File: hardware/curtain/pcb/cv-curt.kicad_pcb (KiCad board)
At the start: 2 copper layers, 88.7 x 99.9 mm, 45 parts, among them J1 2P 5.08mm, J2 3P 5.08mm, K1 SRD-05VDC-SL-C, K2 SRD-05VDC-SL-C, Q1 S8050, Q2 S8050, SW1 Tactile 6mm, SW2 Tactile 6mm, SW3 Tactile 6mm, U1 ESP32-WROOM-32E (4MB), U2 AMS1117-3.3, U3 PC817, U4 PC817

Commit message: hardware: fix mains isolation barrier gaps, add load-controller PCB
Adds the 13th board (ultra-compact dual-channel load controller: ESP32-C3,
opto+relay channel, MOSFET PWM channel, USB-C, AP2112K LDO, USBLC6 ESD) and
regenerates all 12 existing boards, which were stale with respect to earlier
relay-pinout and LED-polarity fixes.

The substantive change is to the mains isolation barrier. It is a keepout band
the router must not cross, deliberately cut where a component straddles it
because there the isolation is provided by the part's package. Three linked
defects made those cuts unsafe, each only visible once the previous was fixed:

1. The cut removed the barrier across the full band width for the straddling
   part's whole height, while the ISO_BRIDGE area that excuses the gap covered
   only the part itself. The router used the leftover strip beside the part to
   bring +5V within 6.99 mm of AC_N against an 8.0 mm reinforced creepage rule.
2. Straddling parts can overlap in y, so cutting per part put one part's
   keepout on another part's pads. The exempt x-ranges are now unioned per
   strip by a sweep line.
3. The rule only relaxes for items insideArea('ISO_BRIDGE'). With the hole the
   same size as the area, a track could hug the hole's edge without being
   contained in it, so the rule fired anyway and the router had no way to know.
   The hole is now the part's pad bbox + 0.3 mm, strictly inside ISO_BRIDGE at
   the footprint bbox + 0.6 mm.

The tighter hole leaves mains nets less room to reach bridge pads, so some
boards report more unconnected items. That is deliberate: those are documented
hand-routing items, whereas a creepage violation is a safety defect.

Also fixed in the generator:
- _pad_shape() derived a pad's layers from PAD::GetLayer(), which returns F.Cu
  even for pads on B.Cu. Every back-side pad became a phantom obstacle on the
  front, blocking legal paths there while hiding the real one behind. Only
  IsOnLayer() is truthful.
- Castella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
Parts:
- moved D2 47.5 mm to (163.7, 164.5)
- moved R2 47.5 mm to (171.8, 154.3)
- moved R5 47.5 mm to (158.6, 157.3)
- moved R8 47.5 mm to (178.4, 163.2)
- moved U2 47.5 mm to (170.3, 166.7)
- moved C2 47.5 mm to (175.6, 154.5)
- moved C3 47.5 mm to (153.0, 136.8)
- moved C4 47.5 mm to (157.5, 136.8)
- moved C5 47.5 mm to (174.6, 151.3)
- moved C6 47.5 mm to (158.6, 154.3)
- moved JP 47.5 mm to (168.2, 154.7)
- moved LED0 47.5 mm to (152.5, 156.3)
- moved LED2 47.5 mm to (152.5, 161.8)
- moved R1 47.5 mm to (179.1, 151.2)
- moved R10 47.5 mm to (153.0, 164.7)
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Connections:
- K1 pad 2: MOTOR_OPEN_PIN_SW -> +5V
- K1 pad 3: +5V -> MOTOR_OPEN_PIN_SW
- K1 pad 4: MOTOR_OPEN_PIN_COIL -> N$K1.4
- K1 pad 5: N$K1.5 -> MOTOR_OPEN_PIN_COIL
- K2 pad 2: MOTOR_CLOSE_PIN_SW -> +5V
- K2 pad 3: +5V -> MOTOR_CLOSE_PIN_SW
- K2 pad 4: MOTOR_CLOSE_PIN_COIL -> N$K2.4
- K2 pad 5: N$K2.5 -> MOTOR_CLOSE_PIN_COIL
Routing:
- net MOTOR_CLOSE_PIN_SW: track 71.5 -> 0.00 mm
- net AC_L_FUSED: track 92.4 -> 23.7 mm
- net AC_N: track 118.4 -> 51.3 mm
- net BTN_STOP: track 88.4 -> 37.5 mm, vias 3 -> 0
- net +3V3: track 193.3 -> 144.2 mm
- net BTN_OPEN: track 104.5 -> 63.2 mm, vias 4 -> 2
- net MOTOR_OPEN_PIN: track 97.8 -> 58.3 mm
- net MOTOR_CLOSE_PIN: track 75.6 -> 45.6 mm, vias 3 -> 1
- net MOTOR_OPEN_PIN_SW: track 28.0 -> 0.00 mm
- net MOTOR_CLOSE_PIN_COIL: track 64.9 -> 49.3 mm
- net BTN_CLOSE: track 77.6 -> 92.9 mm, vias 4 -> 2
- net UART_RX: track 39.3 -> 54.0 mm
- net EN: track 54.6 -> 68.6 mm
- net +5V: track 199.7 -> 188.1 mm, vias 0 -> 1
- net UART_TX: track 44.5 -> 53.2 mm, vias 4 -> 0
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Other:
- outline, holes or cut-outs redrawn
- board text removed: "!! MAINS !!"

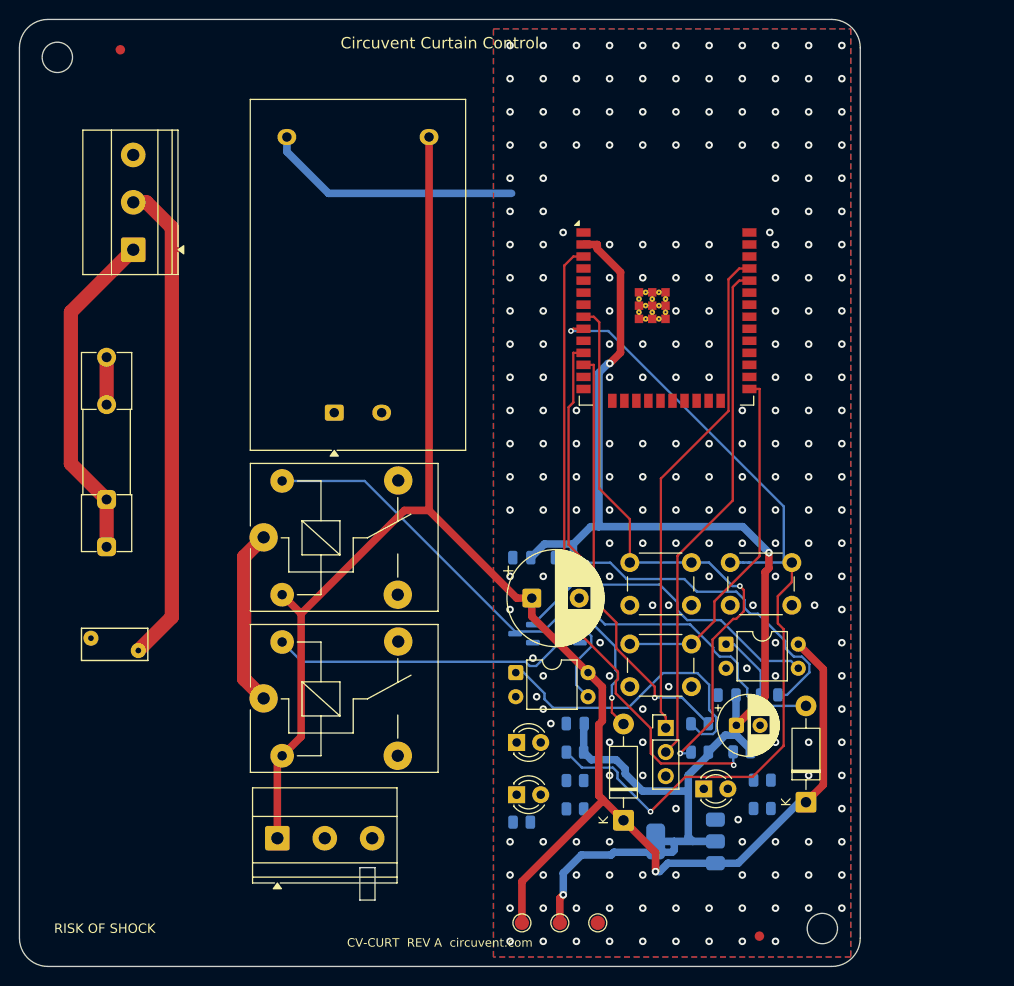
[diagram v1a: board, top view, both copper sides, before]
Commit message: Release 1.10.0, and stop shipping permissions the app never uses
Cut 1.10.0 (versionCode 12) and built it: AAB 38 MB, APK 83 MB, signed with the
upload key, JS bundle embedded.

Checking the generated manifest before writing the Play listing turned up
permissions no one had asked for. Every one of them is printed on the store page
for users to read before they install:

  RECORD_AUDIO          expo-camera asks for the microphone so video can be
                        recorded with sound. This app only ever puts the camera
                        in barcode mode to read a QR label, and expo-speech is
                        output-only - it speaks, it does not listen. Left in,
                        Play lists "Microphone" against a home-control app,
                        which is alarming, unexplainable and untrue.
  SYSTEM_ALERT_WINDOW   React Native's development overlay, useless in a release
                        build and shown to users as "Display over other apps".
  READ/WRITE_EXTERNAL_STORAGE
                        Legacy storage access nothing here touches.

Stripped via android.blockedPermissions. That emits tools:node="remove", which
is a merge instruction rather than a guarantee, so it was checked against the
finished artifact with aapt2 rather than the source manifest - all four are
absent from the APK.

NEARBY_WIFI_DEVICES now carries neverForLocation. Android otherwise treats it as
location-capable, because knowing which networks are in range is enough to place
someone, and Play's data safety review treats it the same way. The app uses it
only to join a new device's setup hotspot. That flag is a promise, so the plugin
says plainly that it has to come off if scan results are ever used positionally.

What is left is defensible: location for Wi-Fi onboarding (Android requires it),
camera for the QR label, nearby-devices flagged as non-positional.

Added mobile/store/listing with the text Play asks for - title, short and full
descriptions, and what'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
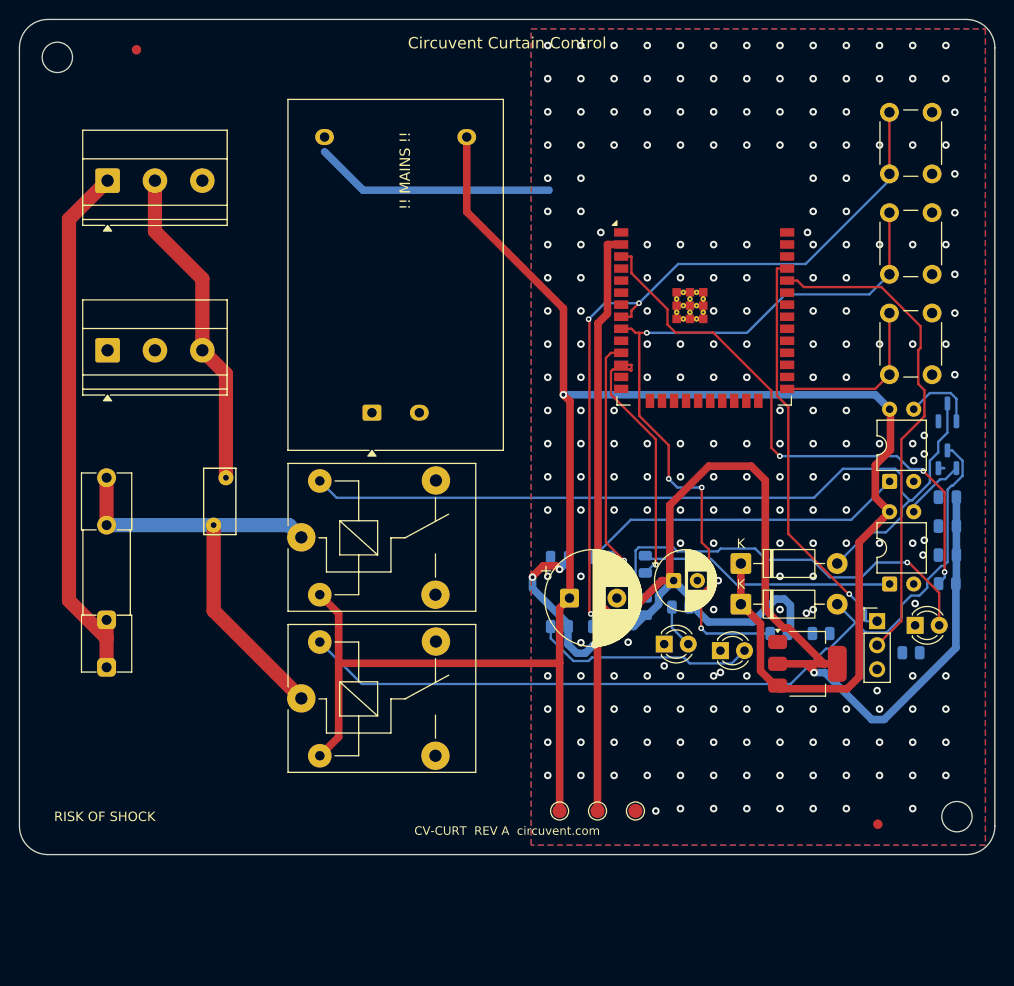
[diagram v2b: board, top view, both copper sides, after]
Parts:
- U2: moved to F.Cu
- moved J2 54.5 mm to (109.3, 114.9)
- moved Q1 50.4 mm to (197.9, 121.5), turned to 90 degrees
- moved SW1 49.3 mm to (191.8, 96.3), turned to 90 degrees
- moved C3 45.3 mm to (197.9, 130.4)
- moved R10 44.8 mm to (194.1, 146.8)
- moved LED0 43.8 mm to (194.5, 143.9)
- moved Q2 43.8 mm to (197.9, 126.4), turned to 90 degrees
- moved C4 40.5 mm to (197.9, 133.4)
- moved U4 40.5 mm to (191.8, 139.6), turned to 90 degrees
- moved SW3 39.5 mm to (191.8, 117.5), turned to 90 degrees
- moved SW2 34.7 mm to (191.8, 106.9), turned to 90 degrees
- moved R9 31.9 mm to (184.6, 144.8)
- moved R3 28.0 mm to (197.9, 139.5)
- moved C5 27.6 mm to (197.9, 136.5)
- moved R6 26.8 mm to (157.0, 144.0)
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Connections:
- J1 pad 3: MOTOR_CLOSE_PIN_SW -> PE
- J2 pad 1: +5V -> MOTOR_OPEN_PIN_SW
- J2 pad 2: MOTOR_OPEN_PIN_SW -> MOTOR_CLOSE_PIN_SW
- LED0 pad 1: N$LED0.1 -> GND
- LED0 pad 2: N$LED0.2 -> LED0_A
- LED1 pad 1: N$LED1.1 -> GND
- LED1 pad 2: N$LED1.2 -> LED1_A
- LED2 pad 1: N$LED2.1 -> GND
- LED2 pad 2: N$LED2.2 -> LED2_A
- R4 pad 2: BTN_OPEN -> LED0_A
- R5 pad 2: BTN_CLOSE -> LED1_A
- R6 pad 1: N$R6.1 -> +3V3
- R6 pad 2: N$R6.2 -> LED2_A
- R7 pad 1: N$R7.1 -> +3V3
- R7 pad 2: N$R7.2 -> BTN_OPEN
- R8 pad 1: N$R8.1 -> +3V3
- R8 pad 2: N$R8.2 -> BTN_CLOSE
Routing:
- net +3V3: track 144.2 -> 203.6 mm, vias 3 -> 4
- net LED0_A: track 0.00 -> 44.5 mm, vias 0 -> 1
- net MOTOR_CLOSE_PIN_COIL: track 49.3 -> 91.7 mm, vias 1 -> 0
- net MOTOR_OPEN_PIN: track 58.3 -> 25.6 mm
- net MOTOR_OPEN_PIN_OPT: track 7.34 -> 34.6 mm
- net MOTOR_OPEN_PIN_DRV: track 33.9 -> 7.83 mm
- net AC_L_FUSED: track 23.7 -> 48.2 mm
- net LED2_A: track 0.00 -> 23.7 mm
- net MOTOR_OPEN_PIN_COIL: track 68.4 -> 89.6 mm
- net AC_L: track 35.6 -> 56.6 mm
- net +5V: track 188.1 -> 207.8 mm
- net BTN_STOP: track 37.5 -> 17.9 mm
- net MOTOR_CLOSE_PIN: track 45.6 -> 27.8 mm
- net BTN_OPEN: track 63.2 -> 80.4 mm, vias 2 -> 3
- net AC_N: track 51.3 -> 34.4 mm
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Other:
- board size 88.7 x 99.9 mm -> 102.9 x 88.1 mm
- board text added: "!! MAINS !!"
